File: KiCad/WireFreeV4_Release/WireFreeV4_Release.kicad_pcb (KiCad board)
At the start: 6 copper layers, 18.9 x 12.1 mm, 43 parts, among them J1 Conn_01x05, J10 Conn_01x01, J11 Conn_01x01, J12 Conn_01x01, J13 Conn_01x01, J14 Conn_01x01, J15 Conn_01x01, J2 Conn_01x25, J3 Conn_01x03, J8 0475710001, U1 TPS62402-Q1, U2 MAX13030EETE+, U3 ATSAME70N21A-CN, Y1 ABM8G-12.000MHZ-4Y-T3

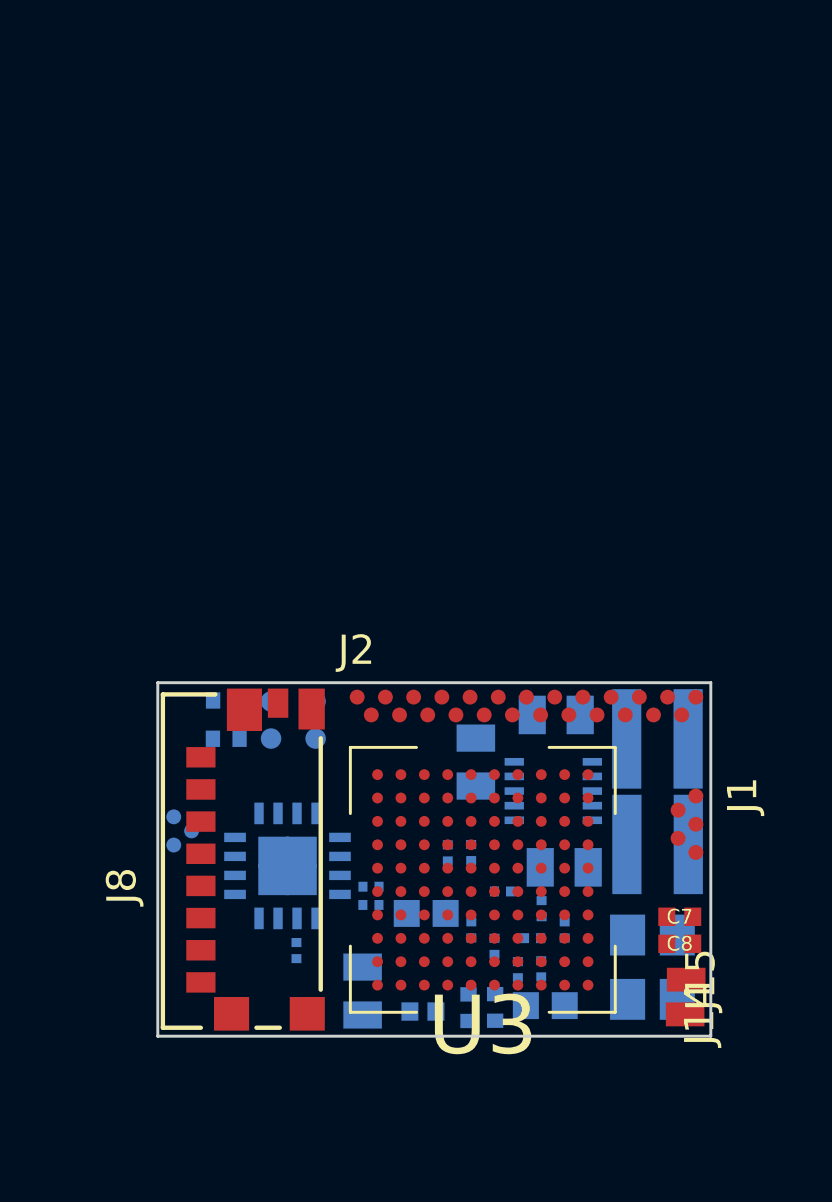
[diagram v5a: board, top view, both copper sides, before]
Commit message: Delete 2 Image Data Lines
1. Delete 2 image data lines from the flexPC cable - now 23 pins

2. Board size: 12.09mm x 18.55mm
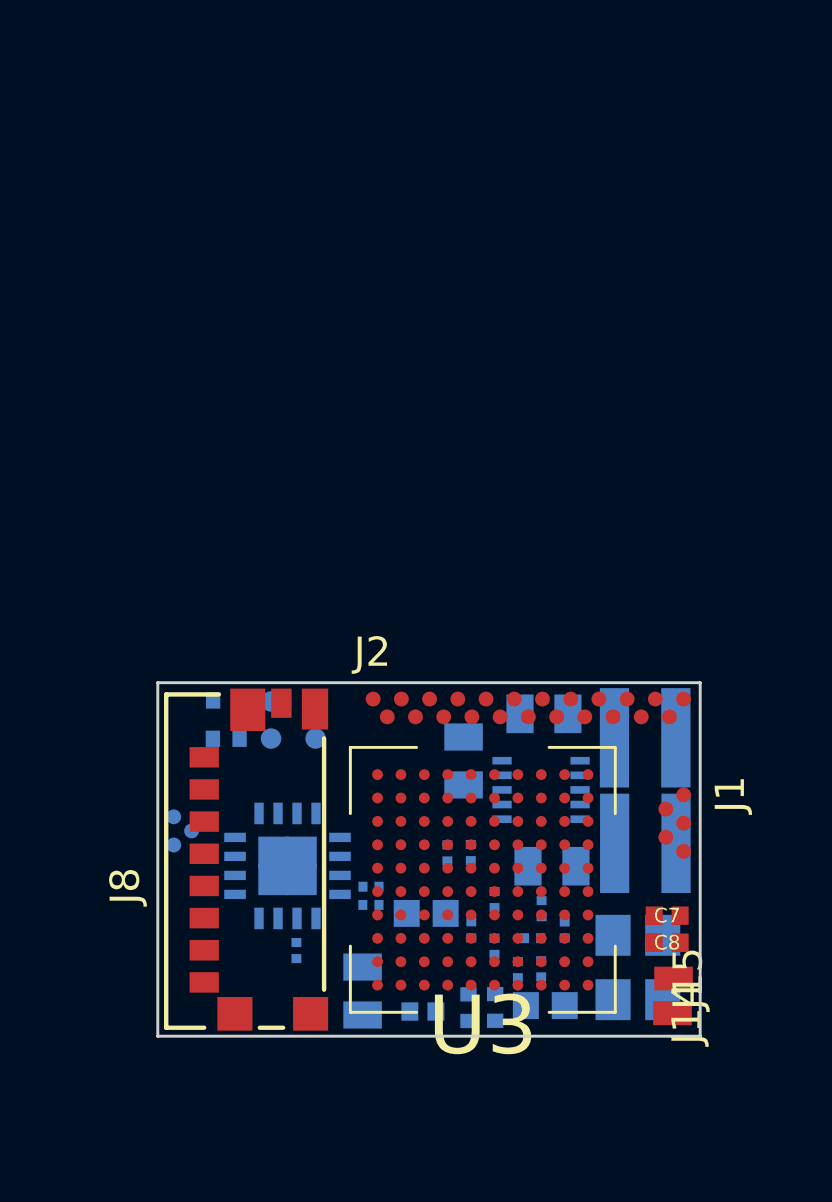
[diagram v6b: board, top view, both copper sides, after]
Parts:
- J2: value Conn_01x25 -> Conn_01x23; footprint .Connector:B2B_Flex_25_Dual_Row_38milx24mil_Pad_20mil -> .Connector:B2B_Flex_23_Dual_Row_38milx24mil_Pad_20mil
- moved J2 0.55 mm to (124.7, 89.2)
- moved Y1 0.50 mm to (133.8, 98.3)
- moved C7 0.43 mm to (134.8, 96.6)
- moved C8 0.43 mm to (134.8, 97.5)
- moved J14 0.43 mm to (135.0, 99.9)
- moved J15 0.43 mm to (135.0, 98.7)
- moved L1 0.42 mm to (134.0, 94.1)
- moved C1 0.42 mm to (127.8, 91.3)
- moved C2 0.42 mm to (130.8, 94.9)
- moved C3 0.42 mm to (130.6, 89.7)
- moved J1 0.42 mm to (135.3, 92.4)
- moved L2 0.42 mm to (134.0, 90.5)
- moved U1 0.42 mm to (130.5, 92.3)
- moved C20 0.39 mm to (128.9, 96.0), turned to 270 degrees
- moved J8 0.11 mm to (118.9, 95.0)
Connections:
- J2 pad 12: /CMOS Imaging Sensor Connectors/img_d8 -> /CMOS Imaging Sensor Connectors/FRAME_VALID
- J2 pad 13: /CMOS Imaging Sensor Connectors/img_d9 -> /CMOS Imaging Sensor Connectors/LINE_VALID
- J2 pad 14: /CMOS Imaging Sensor Connectors/FRAME_VALID -> +3V3
- J2 pad 15: /CMOS Imaging Sensor Connectors/LINE_VALID -> Earth
- J2 pad 16: +3V3 -> /CMOS Imaging Sensor Connectors/Status_LED
- J2 pad 17: Earth -> /CMOS Imaging Sensor Connectors/MOSI
- J2 pad 18: /CMOS Imaging Sensor Connectors/Status_LED -> /CMOS Imaging Sensor Connectors/MISO
- J2 pad 19: /CMOS Imaging Sensor Connectors/MOSI -> /CMOS Imaging Sensor Connectors/MONITOR0
- J2 pad 20: /CMOS Imaging Sensor Connectors/MISO -> /CMOS Imaging Sensor Connectors/TRIGGER0
- J2 pad 21: /CMOS Imaging Sensor Connectors/MONITOR0 -> /CMOS Imaging Sensor Connectors/RESET_N
- J2 pad 22: /CMOS Imaging Sensor Connectors/TRIGGER0 -> /CMOS Imaging Sensor Connectors/SCK
- J2 pad 23: /CMOS Imaging Sensor Connectors/RESET_N -> /CMOS Imaging Sensor Connectors/SS_N
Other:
- board size 18.9 x 12.1 mm -> 18.6 x 12.1 mm

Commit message: Initial Wiring Effort
1. Finish placing vias for the 23-pin.
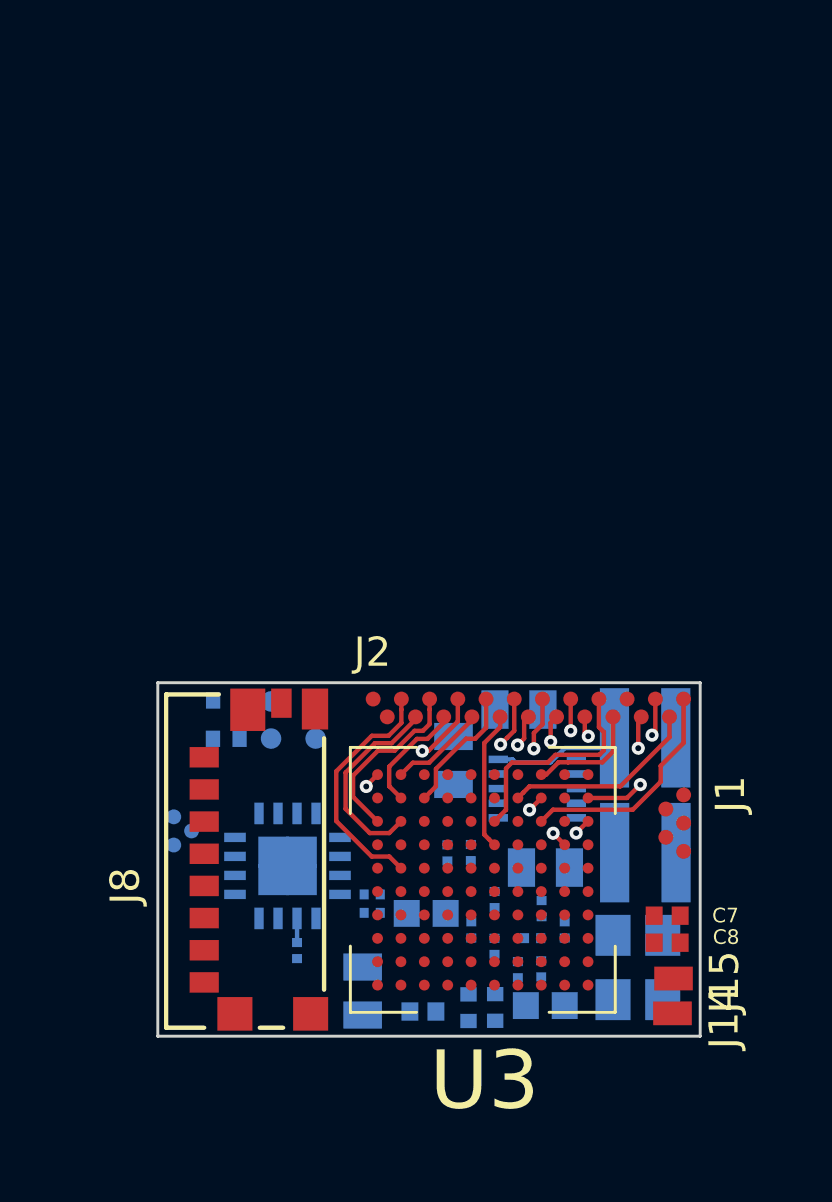
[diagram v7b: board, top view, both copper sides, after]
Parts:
- moved C3 0.87 mm to (129.7, 89.5)
- moved C1 0.35 mm to (127.5, 91.3)
- moved L1 0.32 mm to (134.0, 94.4)
- moved C5 0.27 mm to (124.7, 96.5)
- moved C6 0.27 mm to (124.7, 95.8)
- moved C2 0.23 mm to (130.6, 94.9)
- moved U1 0.13 mm to (130.3, 92.2)
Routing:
- net /CMOS Imaging Sensor Connectors/img_d0: track 0.00 -> 8.31 mm
- net /CMOS Imaging Sensor Connectors/SS_N: track 0.00 -> 7.80 mm
- net /CMOS Imaging Sensor Connectors/MOSI: track 0.00 -> 7.40 mm
- net /CMOS Imaging Sensor Connectors/img_d2: track 0.00 -> 6.87 mm
- net /CMOS Imaging Sensor Connectors/SCK: track 0.00 -> 6.74 mm
- net /CMOS Imaging Sensor Connectors/img_d1: track 0.00 -> 6.12 mm
- net /CMOS Imaging Sensor Connectors/img_d7: track 0.00 -> 4.74 mm
- net /CMOS Imaging Sensor Connectors/img_d5: track 0.00 -> 4.44 mm
- net Net-(L2-Pad1): track 0.00 -> 4.36 mm
- net /CMOS Imaging Sensor Connectors/MISO: track 0.00 -> 3.97 mm
- net /CMOS Imaging Sensor Connectors/img_d3: track 0.00 -> 3.93 mm
- net /CMOS Imaging Sensor Connectors/LINE_VALID: track 0.00 -> 3.80 mm, vias 0 -> 2
- net /CMOS Imaging Sensor Connectors/img_d4: track 0.00 -> 3.31 mm
- net /CMOS Imaging Sensor Connectors/CLK_OUT: track 0.00 -> 2.97 mm, vias 0 -> 2
- net /CMOS Imaging Sensor Connectors/img_d6: track 0.00 -> 2.31 mm, vias 0 -> 2
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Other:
- net class Default: clearance 0.0762 -> 0.1016; trace_width 0.0762 -> 0.0889; via_dia 0.3556 -> 0.45; via_drill 0.1016 -> 0.2
- rule trace_clearance: 0.0762 -> 0.1016
- rule via_min_drill: 0.1016 -> 0.2
- rule via_min_size: 0.254 -> 0.45

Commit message: Release Board Finished (Again)
1. All components, traces and vias placed.

2. Boundaries adjusted to 12.5 mils away from the nearest copper pads.
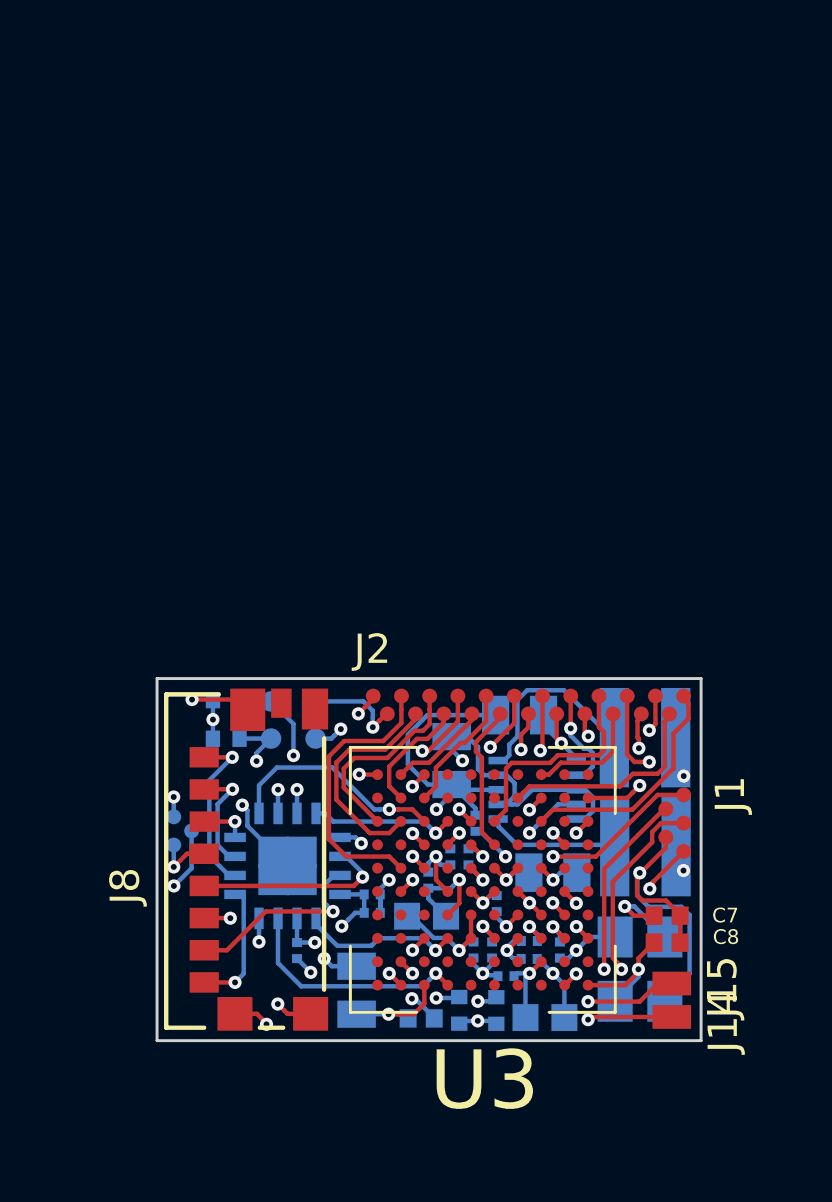
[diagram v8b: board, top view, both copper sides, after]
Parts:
- moved C14 3.69 mm to (128.2, 93.4)
- moved C15 1.34 mm to (126.6, 95.3)
- moved C11 1.23 mm to (129.3, 98.6), turned to 180 degrees
- moved C12 0.71 mm to (131.1, 97.7), turned to 270 degrees
- moved C17 0.69 mm to (128.1, 97.7), turned to 270 degrees
- moved C18 0.53 mm to (130.1, 98.0), turned to 180 degrees
- moved L4 0.41 mm to (130.6, 100.0)
- moved R1 0.33 mm to (127.7, 99.8)
- moved C2 0.31 mm to (130.9, 95.1)
- moved C9 0.24 mm to (126.4, 100.1)
- moved C21 0.21 mm to (124.1, 99.1)
- moved L1 0.21 mm to (134.0, 94.2)
- moved C3 0.19 mm to (129.7, 89.7)
- moved J15 0.18 mm to (134.9, 98.9)
- moved C13 0.17 mm to (127.4, 94.6)
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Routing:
- net Earth: track 1.08 -> 64.6 mm, vias 1 -> 25
- net +BATT: track 0.00 -> 42.9 mm, vias 0 -> 2
- net /External Connectors/SCL: track 0.00 -> 18.9 mm, vias 0 -> 3
- net +1V8: track 0.83 -> 18.1 mm, vias 0 -> 13
- net /External Connectors/IR_Receiver: track 0.00 -> 17.0 mm, vias 0 -> 2
- net /External Connectors/SDA: track 0.00 -> 15.9 mm, vias 0 -> 3
- net /MCU/SD2: track 0.00 -> 13.4 mm, vias 0 -> 2
- net /External Connectors/LED_ENT: track 0.00 -> 11.0 mm, vias 0 -> 2
- net /External Connectors/SWDIO: track 0.00 -> 10.0 mm, vias 0 -> 2
- net /External Connectors/SWDCLK: track 0.00 -> 9.77 mm, vias 0 -> 2
- net +3V3: track 0.93 -> 10.5 mm, vias 1 -> 6
- net /MCU/SDCardCMDA: track 0.00 -> 9.24 mm, vias 0 -> 2
- net +1V2: track 0.00 -> 9.02 mm, vias 0 -> 4
- net /CMOS Imaging Sensor Connectors/MONITOR0: track 0.56 -> 9.56 mm, vias 1 -> 2
- net /MCU/SD1: track 0.00 -> 8.01 mm, vias 0 -> 1
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- added copper zone on In2.Cu, net +1V2
- added copper zone on In4.Cu, net +1V8
- added copper zone on In2.Cu, net +3V3
- added copper zone on In1.Cu, net Earth
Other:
- board size 18.6 x 12.1 mm -> 18.6 x 12.4 mm
